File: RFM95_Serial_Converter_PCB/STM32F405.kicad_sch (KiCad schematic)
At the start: 21 parts, among them SW1 SW_Push, SW2 SW_Push, U6 STM32F405RGTx, Y1 Q13FC1350000200, Y2 X322524MOB4SI

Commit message: Finalised component placement and board edge
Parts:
- Y2: footprint Crystal:Crystal_SMD_3225-4Pin_3.2x2.5mm_HandSoldering -> Crystal:Crystal_SMD_3225-4Pin_3.2x2.5mm
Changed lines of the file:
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@@
     (property "Reference" "Y2" (id 0) (at 257.175 40.64 0))
     (property "Value" "X322524MOB4SI" (id 1) (at 257.81 42.545 0))
-    (property "Footprint" "Crystal:Crystal_SMD_3225-4Pin_3.2x2.5mm_HandSoldering" (id 2) (at 257.175 46.99 0)
+    (property "Footprint" "Crystal:Crystal_SMD_3225-4Pin_3.2x2.5mm" (id 2) (at 257.175 46.99 0)
       (effects (font (size 1.27 1.27)) hide)
     )

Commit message: Routed and ready to order
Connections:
- net USB2_IN-: now reaches R3.2, U6.35 (PB14)
- net USB2_IN+: now reaches R4.2, U6.36 (PB15)
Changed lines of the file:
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@@
+    (effects (font (size 1.27 1.27)) (justify left bottom))
+  )
+  (label "USB2_IN+" (at 182.88 138.43 0)
+    (effects (font (size 1.27 1.27)) (justify left bottom))
+  )
+  (label "USB2_IN-" (at 176.022 135.89 0)
     (effects (font (size 1.27 1.27)) (justify left bottom))
   )

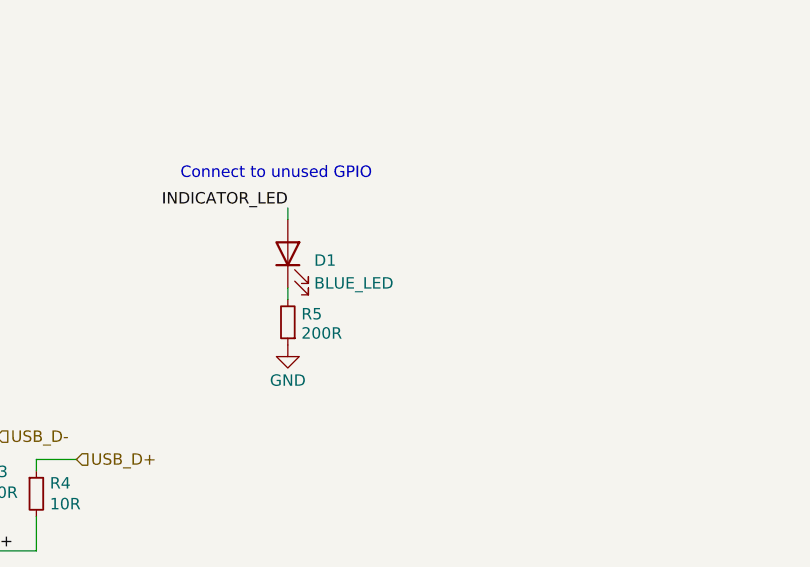
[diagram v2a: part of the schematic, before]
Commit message: Repositioned indicator led and exported step
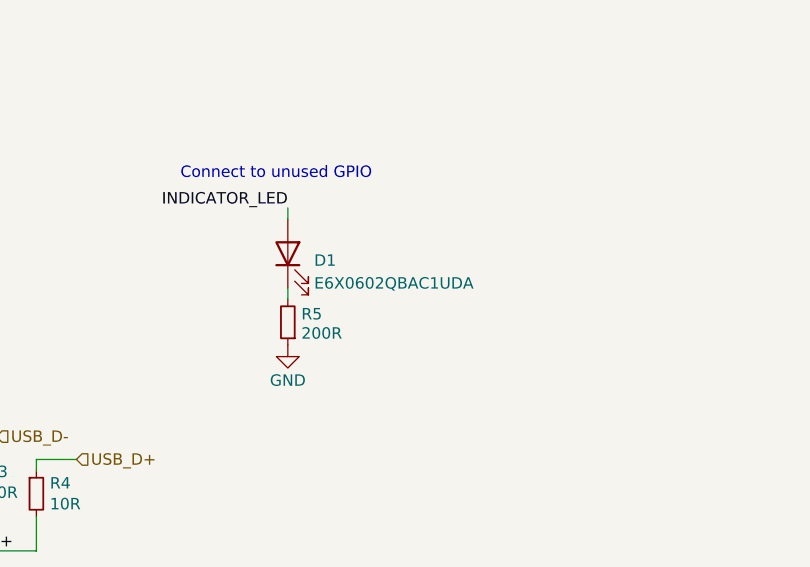
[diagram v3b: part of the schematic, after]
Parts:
- D1: value BLUE_LED -> E6X0602QBAC1UDA
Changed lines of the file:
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@@
       (effects (font (size 1.27 1.27)) (justify right))
     )
-    (property "Value" "BLUE_LED" (id 1) (at 225.171 108.6997 90)
+    (property "Value" "E6X0602QBAC1UDA" (id 1) (at 225.171 108.6997 90)
       (effects (font (size 1.27 1.27)) (justify right))
     )
